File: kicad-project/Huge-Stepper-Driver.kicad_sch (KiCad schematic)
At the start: 4 parts

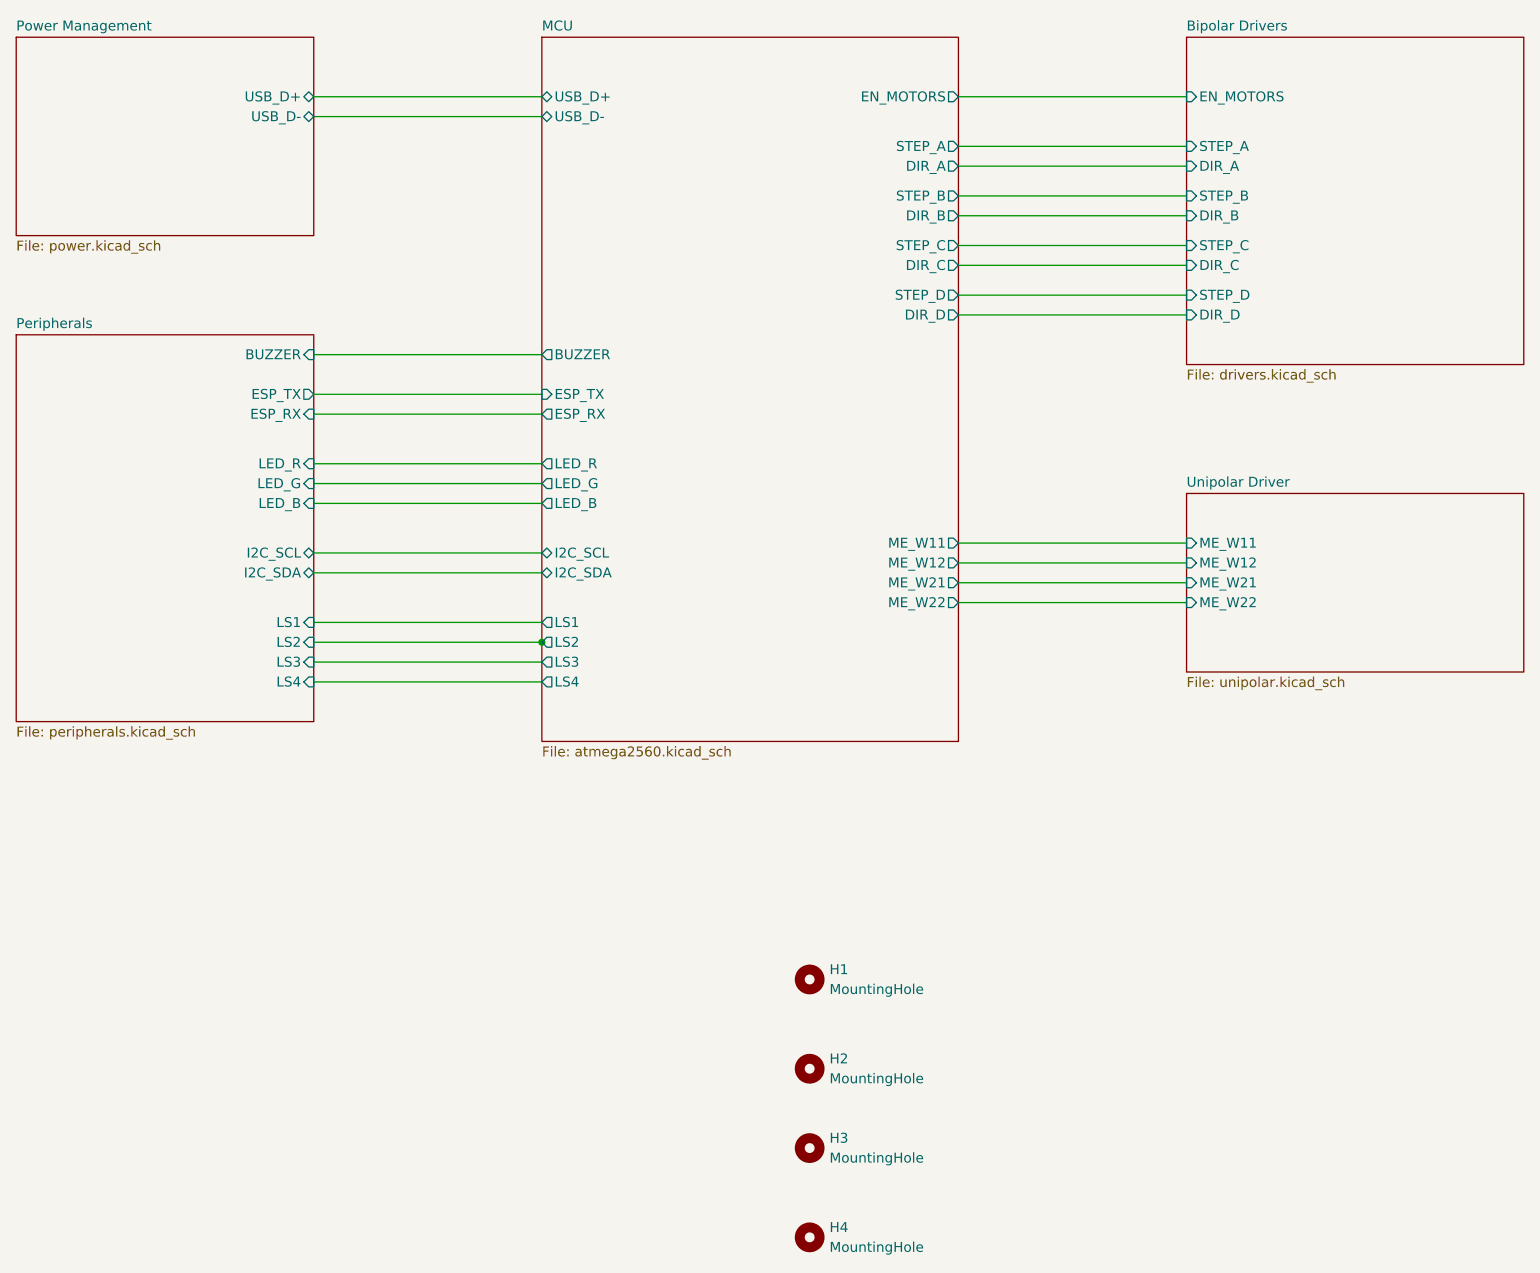
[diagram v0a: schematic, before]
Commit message: hw: finish schematic, PS i2c R_pull-up wrong
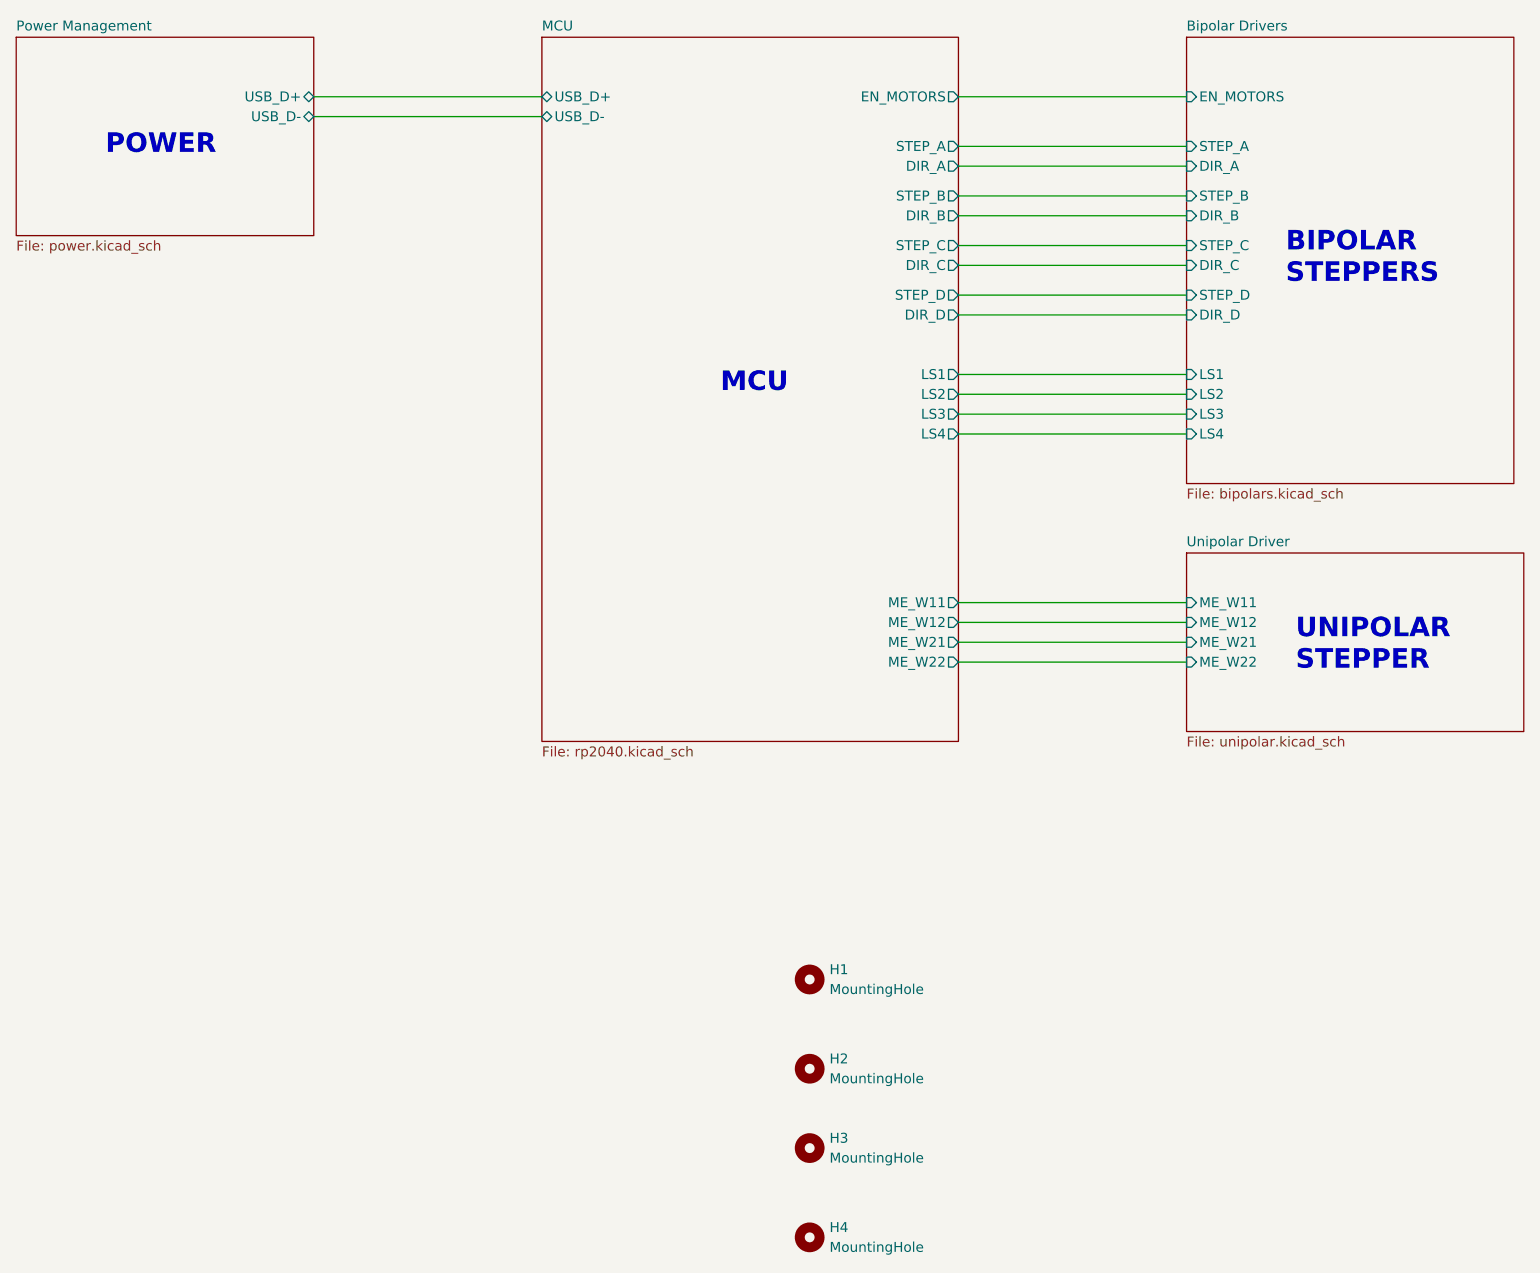
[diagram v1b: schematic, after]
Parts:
- H1, H2, H3, H4: footprint (none) -> MountingHole:MountingHole_3.2mm_M3
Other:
- removed sheet Peripherals
- sheet Bipolar Drivers: file drivers.kicad_sch -> bipolars.kicad_sch
- sheet Bipolar Drivers ports: added LS1, LS2, LS3, LS4; removed none
- sheet MCU: file atmega2560.kicad_sch -> rp2040.kicad_sch
- sheet MCU ports: added none; removed BUZZER, ESP_RX, ESP_TX, I2C_SCL, I2C_SDA, LED_B, LED_G, LED_R
- note added: "BIPOLAR STEPPERS"
- note added: "MCU"
- note added: "POWER"
- note added: "UNIPOLAR STEPPER"
